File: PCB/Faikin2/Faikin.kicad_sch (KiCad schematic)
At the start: 31 parts, among them J1 1x5, J2 Shelly, J3 USB-PROG, Q1 BSS138PS, U2 ESP32-S3-MINI-1, U3 MD8942

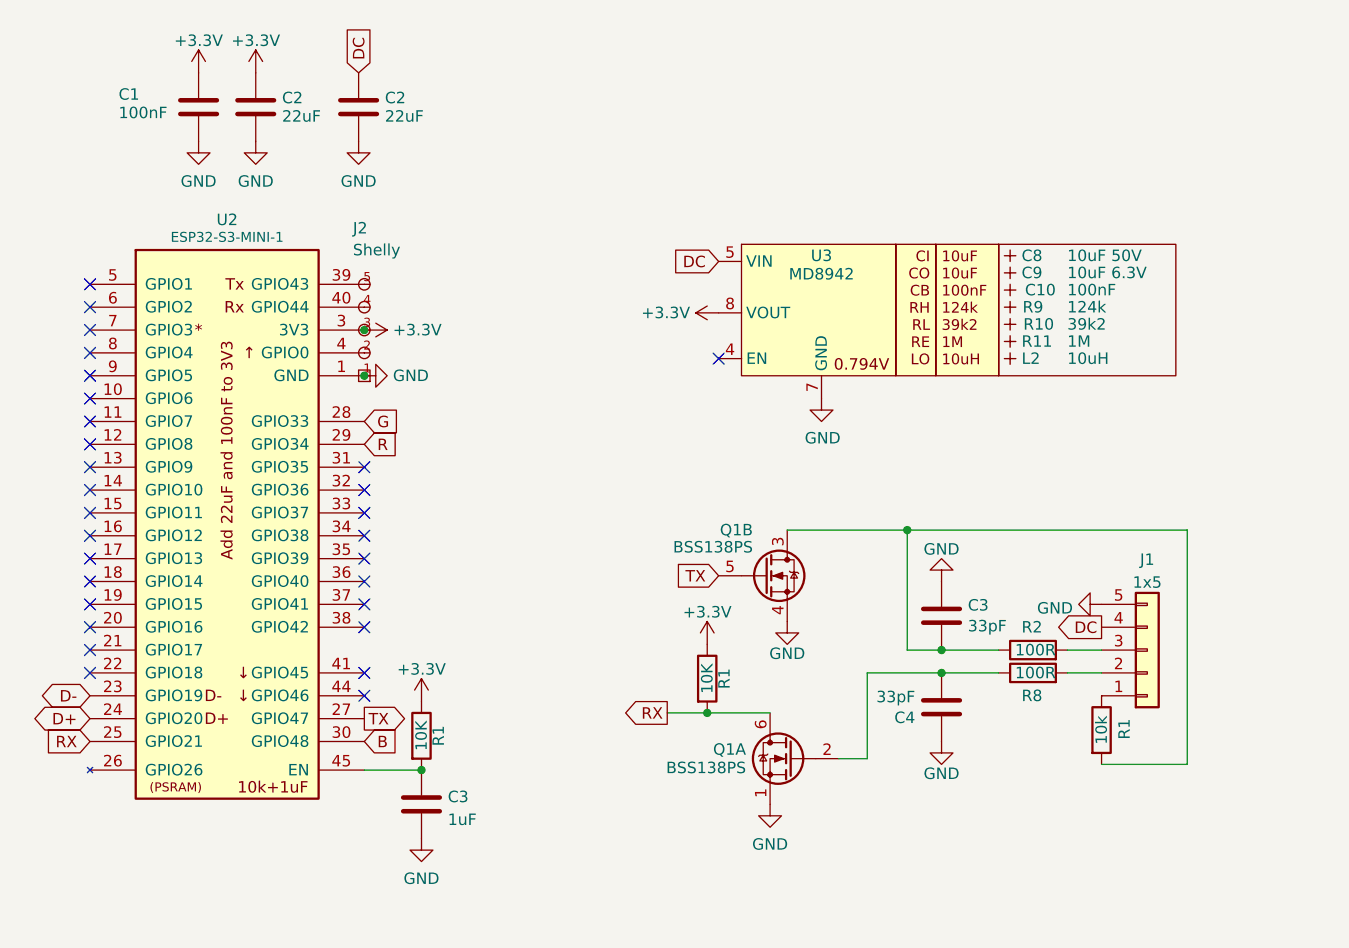
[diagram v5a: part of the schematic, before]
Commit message: Clean up to reduce noise
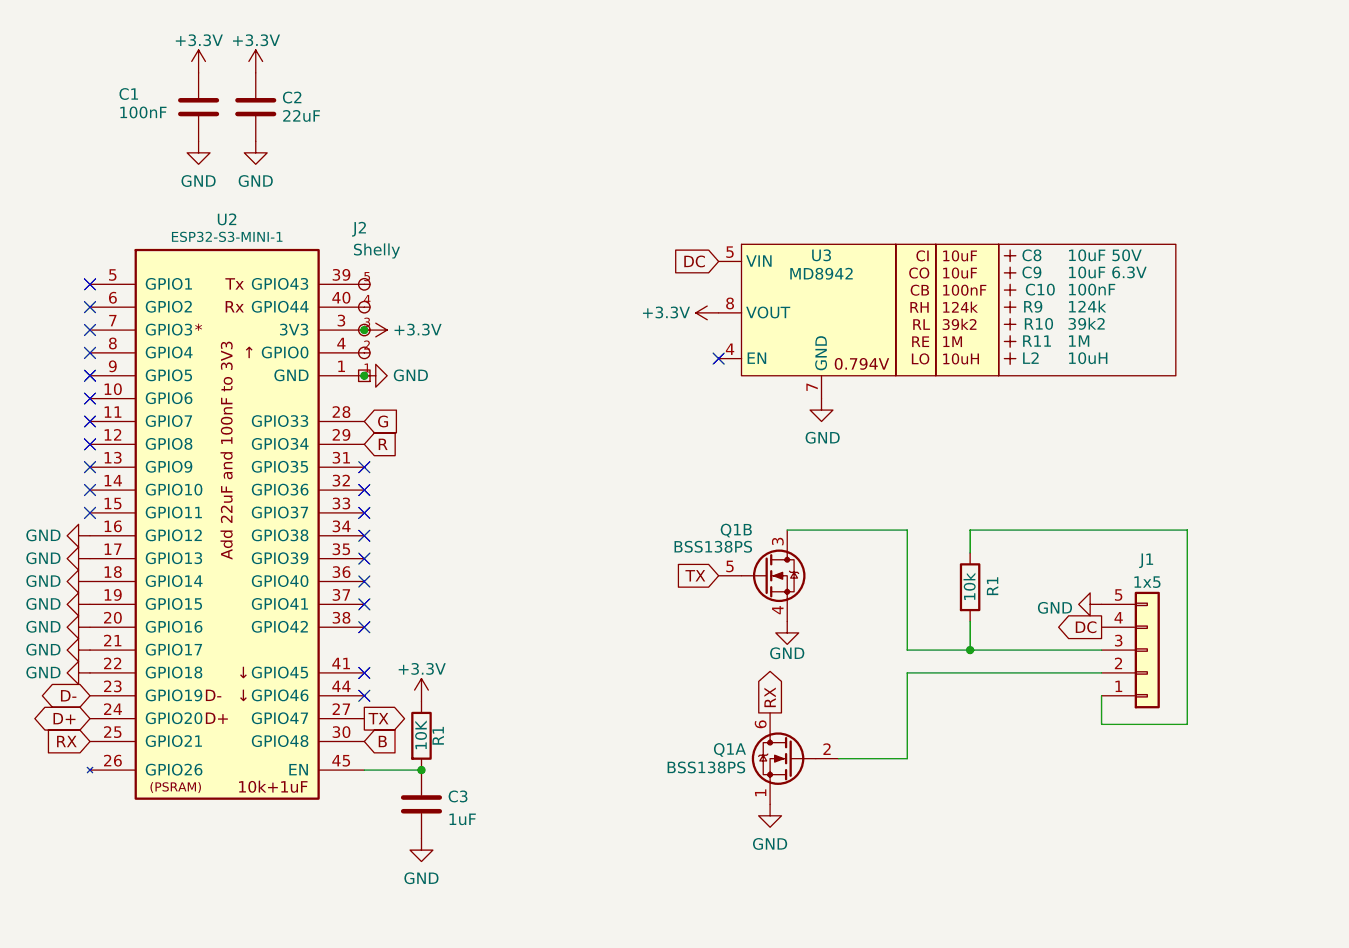
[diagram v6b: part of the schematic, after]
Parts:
- removed C2: 22uF, RevK:C_0402, symbol Device:C
- removed C3, C4: 33pF, RevK:C_0402, symbol Device:C
- removed R1: 10K, RevK:R_0402, symbol Device:R
- removed R2, R8: 100R, RevK:R_0402, symbol Device:R
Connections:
- net GND: now also U2.16 (GPIO12), U2.17 (GPIO13), U2.18 (GPIO14), U2.19 (GPIO15), U2.20 (GPIO16), U2.21 (GPIO17), U2.22 (GPIO18)
- net at Q1.2 (GN): now also J1.2 (Pin_2)
- net at Q1.3 (SP), R1.2: now also J1.3 (Pin_3)
- no-connect marks 29 -> 22
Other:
- moved on the sheet: R1

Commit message: Added cap
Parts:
- added C1: 100nF, RevK:C_0402, symbol Device:C
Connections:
- net GND: now also C1.2
- net at J1.2 (Pin_2), Q1.2 (GN): now also C1.1
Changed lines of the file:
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@@
   (junction (at 79.375 53.34) (diameter 0) (color 0 0 0 0)
+  )
+  (junction (at 146.685 91.44) (diameter 0) (color 0 0 0 0)
   )
   (junction (at 79.375 58.42) (diameter 0) (color 0 0 0 0)
@@
     (stroke (width 0) (type default))
   )
-  (wire (pts (xy 139.7 91.44) (xy 161.29 91.44))
+  (wire (pts (xy 139.7 91.44) (xy 146.685 91.44))
     (stroke (width 0) (type default))
   )
@@
   )
   (wire (pts (xy 139.7 91.44) (xy 139.7 100.965))
+    (stroke (width 0) (type default))
+  )
+  (wire (pts (xy 146.685 91.44) (xy 161.29 91.44))
     (stroke (width 0) (type default))
   )
@@
         (path "/46c350bb-7de4-4e81-aafd-4af55e37aab0"
           (reference "#PWR09") (unit 1)
+        )
+      )
+    )
+  )
+  (symbol (lib_id "power:GND") (at 146.685 99.06 0) (unit 1)
+    (in_bom yes) (on_board yes) (dnp no) (fields_autoplaced)
+    (property "Reference" "#PWR022" (at 146.685 105.41 0)
+      (effects (font (size 1.27 1.27)) hide)
+    )
+    (property "Value" "GND" (at 146.685 103.5034 0)
+      (effects (font (size 1.27 1.27)))
+    )
+    (property "Footprint" "" (at 146.685 99.06 0)
+      (effects (font (size 1.27 1.27)) hide)
+    )
+    (property "Datasheet" "" (at 146.685 99.06 0)
+      (effects (font (size 1.27 1.27)) hide)
+    )
+    (pin "1")
+    (instances
+      (project "Faikin"
+        (path "/46c350bb-7de4-4e81-aafd-4af55e37aab0"
+          (reference "#PWR022") (unit 1)
         )
       )
@@
         )
       )
+    )
+  )
+  (symbol (lib_id "Device:C") (at 146.685 95.25 0) (unit 1)
+    (in_bom yes) (on_board yes) (dnp no)
+    (property "Reference" "C1" (at 149.86 93.837 0)
+      (effects (font (size 1.27 1.27)) (justify left))
+    )
+    (property "Value" "100nF" (at 149.86 95.885 0)
+      (effects (font (size 1.27 1.27)) (justify left))
+    )
+    (property "Footprint" "RevK:C_0402" (at 147.6502 99.06 0)
+      (effects (font (size 1.27 1.27)) hide)
+    )
+    (property "Datasheet" "~" (at 146.685 95.25 0)
+      (effects (font (size 1.27 1.27)) hide)
+    )
+    (pin "1")
+    (pin "2")
+    (instances
+      (project "USBA"
+        (path "/2d210a96-f81f-42a9-8bf4-1b43c11086f3"
+          (reference "C1") (unit 1)
+        )
+      )
+      (project "Faikin"
+        (path "/46c350bb-7de4-4e81-aafd-4af55e37aab0"
+          (reference "C1") (unit 1)
+        )
+      )

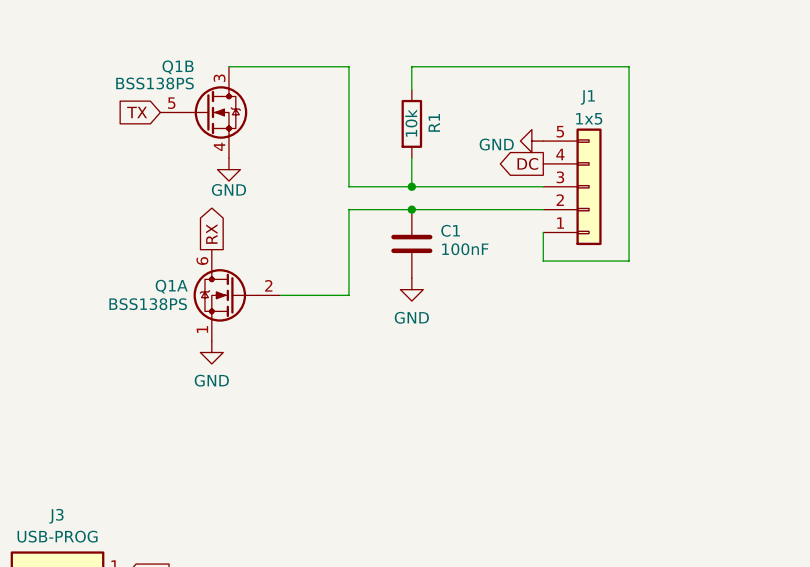
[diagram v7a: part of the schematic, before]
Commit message: Removed cap, tests show it makes matters worse
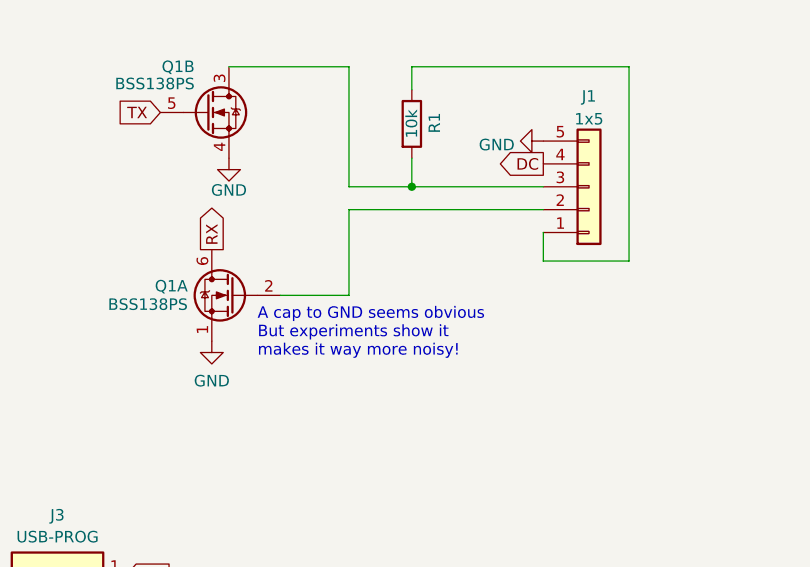
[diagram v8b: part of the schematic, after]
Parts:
- removed C1: 100nF, RevK:C_0402, symbol Device:C
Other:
- note added: "A cap to GND seems obvious But experiments show it makes it way more noisy!"
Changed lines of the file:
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@@
   (junction (at 79.375 53.34) (diameter 0) (color 0 0 0 0)
-  )
-  (junction (at 146.685 91.44) (diameter 0) (color 0 0 0 0)
   )
   (junction (at 79.375 58.42) (diameter 0) (color 0 0 0 0)
@@
     (stroke (width 0) (type default))
   )
-  (wire (pts (xy 139.7 91.44) (xy 146.685 91.44))
+  (wire (pts (xy 139.7 91.44) (xy 161.29 91.44))
     (stroke (width 0) (type default))
   )
@@
     (stroke (width 0) (type default))
   )
-  (wire (pts (xy 146.685 91.44) (xy 161.29 91.44))
-    (stroke (width 0) (type default))
-  )
   (wire (pts (xy 139.7 75.565) (xy 139.7 88.9))
     (stroke (width 0) (type default))
@@
   (wire (pts (xy 146.685 78.105) (xy 146.685 75.565))
     (stroke (width 0) (type default))
+  )
+  (text "A cap to GND seems obvious\nBut experiments show it\nmakes it way more noisy!"
+    (at 129.54 107.95 0)
+    (effects (font (size 1.27 1.27)) (justify left bottom))
   )
   (global_label "DC" (shape input) (at 114.935 132.08 0) (fields_autoplaced)
@@
         (path "/46c350bb-7de4-4e81-aafd-4af55e37aab0"
           (reference "#PWR09") (unit 1)
-        )
-      )
-    )
-  )
-  (symbol (lib_id "power:GND") (at 146.685 99.06 0) (unit 1)
-    (in_bom yes) (on_board yes) (dnp no) (fields_autoplaced)
-    (property "Reference" "#PWR022" (at 146.685 105.41 0)
-      (effects (font (size 1.27 1.27)) hide)
-    )
-    (property "Value" "GND" (at 146.685 103.5034 0)
-      (effects (font (size 1.27 1.27)))
-    )
-    (property "Footprint" "" (at 146.685 99.06 0)
-      (effects (font (size 1.27 1.27)) hide)
-    )
-    (property "Datasheet" "" (at 146.685 99.06 0)
-      (effects (font (size 1.27 1.27)) hide)
-    )
-    (pin "1")
-    (instances
-      (project "Faikin"
-        (path "/46c350bb-7de4-4e81-aafd-4af55e37aab0"
-          (reference "#PWR022") (unit 1)
         )
       )
@@
         )
       )
-    )
-  )
-  (symbol (lib_id "Device:C") (at 146.685 95.25 0) (unit 1)
-    (in_bom yes) (on_board yes) (dnp no)
-    (property "Reference" "C1" (at 149.86 93.837 0)
-      (effects (font (size 1.27 1.27)) (justify left))
-    )
-    (property "Value" "100nF" (at 149.86 95.885 0)
-      (effects (font (size 1.27 1.27)) (justify left))
-    )
-    (property "Footprint" "RevK:C_0402" (at 147.6502 99.06 0)
-      (effects (font (size 1.27 1.27)) hide)
-    )
-    (property "Datasheet" "~" (at 146.685 95.25 0)
-      (effects (font (size 1.27 1.27)) hide)
-    )
-    (pin "1")
-    (pin "2")
-    (instances
-      (project "USBA"
-        (path "/2d210a96-f81f-42a9-8bf4-1b43c11086f3"
-          (reference "C1") (unit 1)
-        )
-      )
-      (project "Faikin"
-        (path "/46c350bb-7de4-4e81-aafd-4af55e37aab0"
-          (reference "C1") (unit 1)
-        )
-      )
